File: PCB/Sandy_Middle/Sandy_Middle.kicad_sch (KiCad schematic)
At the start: 80 parts, among them J1 Conn_02x02_Top_Bottom, J2 Conn_02x02_Top_Bottom, J3 Conn_02x02_Top_Bottom

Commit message: ネジ穴のフットプリントをわかりやすく
これまでKiCadのライブラリに保存していたフットプリントを、ローカルへ移動。
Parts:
- H1, H10, H11, H12, H13, H14, H15, H16, H17, H18, H19, H2, H3, H4, H5, H6, H7, H8, H9: footprint MountingHole:MountingHole_2.2mm_M2_Pad_minimal -> locallib:MountingHole_2.2mm_M2_Pad_minimal

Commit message: ダイオードの方向を強調するシルクに変更
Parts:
- D1, D10, D11, D12, D13, D14, D15, D16, D17, D18, D2, D3, D4, D5, D6, D7, D8, D9: footprint Diode_SMD:D_SOD-123 -> locallib:D_SOD-123_Emphasized_Direction_Line
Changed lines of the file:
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@@
       (effects (font (size 1.27 1.27)) (justify right))
     )
-    (property "Footprint" "Diode_SMD:D_SOD-123" (id 2) (at 262.89 78.74 0)
+    (property "Footprint" "locallib:D_SOD-123_Emphasized_Direction_Line" (id 2) (at 262.89 78.74 0)
       (effects (font (size 1.27 1.27)) hide)
     )
@@
       (effects (font (size 1.27 1.27)) (justify right))
     )
-    (property "Footprint" "Diode_SMD:D_SOD-123" (id 2) (at 180.34 110.49 0)
+    (property "Footprint" "locallib:D_SOD-123_Emphasized_Direction_Line" (id 2) (at 180.34 110.49 0)
       (effects (font (size 1.27 1.27)) hide)
     )
@@
       (effects (font (size 1.27 1.27)) (justify right))
     )
-    (property "Footprint" "Diode_SMD:D_SOD-123" (id 2) (at 114.3 78.74 0)
+    (property "Footprint" "locallib:D_SOD-123_Emphasized_Direction_Line" (id 2) (at 114.3 78.74 0)
       (effects (font (size 1.27 1.27)) hide)
     )
@@
       (effects (font (size 1.27 1.27)) (justify right))
     )
-    (property "Footprint" "Diode_SMD:D_SOD-123" (id 2) (at 147.32 142.24 0)
+    (property "Footprint" "locallib:D_SOD-123_Emphasized_Direction_Line" (id 2) (at 147.32 142.24 0)
       (effects (font (size 1.27 1.27)) hide)
     )
@@
       (effects (font (size 1.27 1.27)) (justify right))
     )
-    (property "Footprint" "Diode_SMD:D_SOD-123" (id 2) (at 147.32 110.49 0)
+    (property "Footprint" "locallib:D_SOD-123_Emphasized_Direction_Line" (id 2) (at 147.32 110.49 0)
       (effects (font (size 1.27 1.27)) hide)
     )
@@
       (effects (font (size 1.27 1.27)) (justify right))
     )
-    (property "Footprint" "Diode_SMD:D_SOD-123" (id 2) (at 350.52 211.455 0)
+    (property "Footprint" "locallib:D_SOD-123_Emphasized_Direction_Line" (id 2) (at 350.52 211.455 0)
       (effects (font (size 1.27 1.27)) hide)
     )
@@
       (effects (font (size 1.27 1.27)) (justify right))
     )
-    (property "Footprint" "Diode_SMD:D_SOD-123" (id 2) (at 246.38 78.74 0)
+    (property "Footprint" "locallib:D_SOD-123_Emphasized_Direction_Line" (id 2) (at 246.38 78.74 0)
       (effects (font (size 1.27 1.27)) hide)
     )
@@
       (effects (font (size 1.27 1.27)) (justify right))
     )
-    (property "Footprint" "Diode_SMD:D_SOD-123" (id 2) (at 196.85 78.74 0)
+    (property "Footprint" "locallib:D_SOD-123_Emphasized_Direction_Line" (id 2) (at 196.85 78.74 0)
       (effects (font (size 1.27 1.27)) hide)
     )
@@
       (effects (font (size 1.27 1.27)) (justify right))
     )
-    (property "Footprint" "Diode_SMD:D_SOD-123" (id 2) (at 383.54 208.915 0)
+    (property "Footprint" "locallib:D_SOD-123_Emphasized_Direction_Line" (id 2) (at 383.54 208.915 0)
       (effects (font (size 1.27 1.27)) hide)
     )
@@
       (effects (font (size 1.27 1.27)) (justify right))
     )
-    (property "Footprint" "Diode_SMD:D_SOD-123" (id 2) (at 180.34 142.24 0)
+    (property "Footprint" "locallib:D_SOD-123_Emphasized_Direction_Line" (id 2) (at 180.34 142.24 0)
       (effects (font (size 1.27 1.27)) hide)
     )
@@
       (effects (font (size 1.27 1.27)) (justify right))
     )
-    (property "Footprint" "Diode_SMD:D_SOD-123" (id 2) (at 64.77 78.74 0)
+    (property "Footprint" "locallib:D_SOD-123_Emphasized_Direction_Line" (id 2) (at 64.77 78.74 0)
       (effects (font (size 1.27 1.27)) hide)
     )
@@
       (effects (font (size 1.27 1.27)) (justify right))
     )
-    (property "Footprint" "Diode_SMD:D_SOD-123" (id 2) (at 130.81 110.49 0)
+    (property "Footprint" "locallib:D_SOD-123_Emphasized_Direction_Line" (id 2) (at 130.81 110.49 0)
       (effects (font (size 1.27 1.27)) hide)
     )
@@
       (effects (font (size 1.27 1.27)) (justify right))
     )
-    (property "Footprint" "Diode_SMD:D_SOD-123" (id 2) (at 48.26 78.74 0)
+    (property "Footprint" "locallib:D_SOD-123_Emphasized_Direction_Line" (id 2) (at 48.26 78.74 0)
       (effects (font (size 1.27 1.27)) hide)
     )
@@
       (effects (font (size 1.27 1.27)) (justify right))
     )
-    (property "Footprint" "Diode_SMD:D_SOD-123" (id 2) (at 391.16 206.375 0)
+    (property "Footprint" "locallib:D_SOD-123_Emphasized_Direction_Line" (id 2) (at 391.16 206.375 0)
       (effects (font (size 1.27 1.27)) hide)
     )
@@
       (effects (font (size 1.27 1.27)) (justify right))
     )
-    (property "Footprint" "Diode_SMD:D_SOD-123" (id 2) (at 342.9 208.915 0)
+    (property "Footprint" "locallib:D_SOD-123_Emphasized_Direction_Line" (id 2) (at 342.9 208.915 0)
       (effects (font (size 1.27 1.27)) hide)
     )
@@
       (effects (font (size 1.27 1.27)) (justify right))
     )
-    (property "Footprint" "Diode_SMD:D_SOD-123" (id 2) (at 375.92 211.455 0)
+    (property "Footprint" "locallib:D_SOD-123_Emphasized_Direction_Line" (id 2) (at 375.92 211.455 0)
       (effects (font (size 1.27 1.27)) hide)
     )
@@
       (effects (font (size 1.27 1.27)) (justify right))
     )
-    (property "Footprint" "Diode_SMD:D_SOD-123" (id 2) (at 163.83 142.24 0)
+    (property "Footprint" "locallib:D_SOD-123_Emphasized_Direction_Line" (id 2) (at 163.83 142.24 0)
       (effects (font (size 1.27 1.27)) hide)
     )
@@
       (effects (font (size 1.27 1.27)) (justify right))
     )
-    (property "Footprint" "Diode_SMD:D_SOD-123" (id 2) (at 163.83 110.49 0)
+    (property "Footprint" "locallib:D_SOD-123_Emphasized_Direction_Line" (id 2) (at 163.83 110.49 0)
       (effects (font (size 1.27 1.27)) hide)
     )
@@
     )
     (path "/98a572f1-8857-4d32-9682-98d5a690baab"
-      (reference "D1") (unit 1) (value "D") (footprint "Diode_SMD:D_SOD-123")
+      (reference "D1") (unit 1) (value "D") (footprint "locallib:D_SOD-123_Emphasized_Direction_Line")
     )
     (path "/79b01d85-3e7e-49a5-baa8-c54e7a8ce4fa"
-      (reference "D2") (unit 1) (value "D") (footprint "Diode_SMD:D_SOD-123")
+      (reference "D2") (unit 1) (value "D") (footprint "locallib:D_SOD-123_Emphasized_Direction_Line")
     )
     (path "/10264225-1791-410d-9e41-7749c3624088"
-      (reference "D3") (unit 1) (value "D") (footprint "Diode_SMD:D_SOD-123")
+      (reference "D3") (unit 1) (value "D") (footprint "locallib:D_SOD-123_Emphasized_Direction_Line")
     )
     (path "/372e4b73-5697-4558-8707-c0918e154230"
-      (reference "D4") (unit 1) (value "D") (footprint "Diode_SMD:D_SOD-123")
+      (reference "D4") (unit 1) (value "D") (footprint "locallib:D_SOD-123_Emphasized_Direction_Line")
     )
     (path "/1e52539e-b1ab-4d88-9790-3c1108cb980e"
-      (reference "D5") (unit 1) (value "D") (footprint "Diode_SMD:D_SOD-123")
+      (reference "D5") (unit 1) (value "D") (footprint "locallib:D_SOD-123_Emphasized_Direction_Line")
     )
     (path "/02eb5dc3-9dab-4bdb-8773-510daf46eb56"
-      (reference "D6") (unit 1) (value "D") (footprint "Diode_SMD:D_SOD-123")
+      (reference "D6") (unit 1) (value "D") (footprint "locallib:D_SOD-123_Emphasized_Direction_Line")
     )
     (path "/7f4aa78f-d5fa-4df8-b529-c2e308c53e79"
-      (reference "D7") (unit 1) (value "D") (footprint "Diode_SMD:D_SOD-123")
+      (reference "D7") (unit 1) (value "D") (footprint "locallib:D_SOD-123_Emphasized_Direction_Line")
     )
     (path "/114f479f-c6d8-46a0-bd29-052d023e9b3d"
-      (reference "D8") (unit 1) (value "D") (footprint "Diode_SMD:D_SOD-123")
+      (reference "D8") (unit 1) (value "D") (footprint "locallib:D_SOD-123_Emphasized_Direction_Line")
     )
     (path "/fea2466c-e6a8-4101-8437-6f750141ce2c"
-      (reference "D9") (unit 1) (value "D") (footprint "Diode_SMD:D_SOD-123")
+      (reference "D9") (unit 1) (value "D") (footprint "locallib:D_SOD-123_Emphasized_Direction_Line")
     )
     (path "/05274209-3705-4225-9924-d5d2588282b9"
-      (reference "D10") (unit 1) (value "D") (footprint "Diode_SMD:D_SOD-123")
+      (reference "D10") (unit 1) (value "D") (footprint "locallib:D_SOD-123_Emphasized_Direction_Line")
     )
     (path "/114627db-0c52-4502-94e0-058f1357fd45"
-      (reference "D11") (unit 1) (value "D") (footprint "Diode_SMD:D_SOD-123")
+      (reference "D11") (unit 1) (value "D") (footprint "locallib:D_SOD-123_Emphasized_Direction_Line")
     )
     (path "/e73a99b3-45a4-48e4-b59e-5c57a9a725ce"
-      (reference "D12") (unit 1) (value "D") (footprint "Diode_SMD:D_SOD-123")
+      (reference "D12") (unit 1) (value "D") (footprint "locallib:D_SOD-123_Emphasized_Direction_Line")
     )
     (path "/40013a98-70f3-4e35-90ce-3840d3806235"
-      (reference "D13") (unit 1) (value "D") (footprint "Diode_SMD:D_SOD-123")
+      (reference "D13") (unit 1) (value "D") (footprint "locallib:D_SOD-123_Emphasized_Direction_Line")
     )
     (path "/9f424bf6-d591-4ef8-ab26-5de921e524da"
-      (reference "D14") (unit 1) (value "D") (footprint "Diode_SMD:D_SOD-123")
+      (reference "D14") (unit 1) (value "D") (footprint "locallib:D_SOD-123_Emphasized_Direction_Line")
     )
     (path "/a92d7c5f-b604-465e-a4c5-bd808af5ea5f"
-      (reference "D15") (unit 1) (value "D") (footprint "Diode_SMD:D_SOD-123")
+      (reference "D15") (unit 1) (value "D") (footprint "locallib:D_SOD-123_Emphasized_Direction_Line")
     )
     (path "/3c9dd9f6-196b-4ea2-bd2f-322451f5fe46"
-      (reference "D16") (unit 1) (value "D") (footprint "Diode_SMD:D_SOD-123")
+      (reference "D16") (unit 1) (value "D") (footprint "locallib:D_SOD-123_Emphasized_Direction_Line")
     )
     (path "/1680d709-e50f-4ff9-ada3-4903ce086e07"
-      (reference "D17") (unit 1) (value "D") (footprint "Diode_SMD:D_SOD-123")
+      (reference "D17") (unit 1) (value "D") (footprint "locallib:D_SOD-123_Emphasized_Direction_Line")
     )
     (path "/af171445-bb08-40d9-9b16-1214459bb813"
-      (reference "D18") (unit 1) (value "D") (footprint "Diode_SMD:D_SOD-123")
+      (reference "D18") (unit 1) (value "D") (footprint "locallib:D_SOD-123_Emphasized_Direction_Line")
     )
     (path "/957451e1-7977-4bf5-b4a7-01d7dbc16c20"

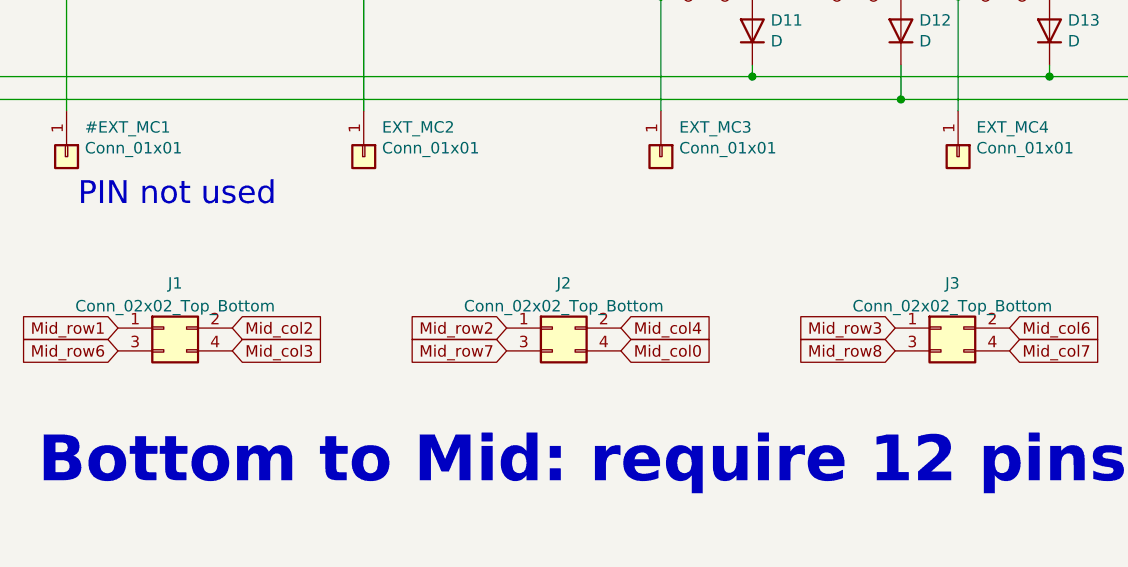
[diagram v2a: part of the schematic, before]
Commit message: コネクタの番号と、パーツの番号を合わせる
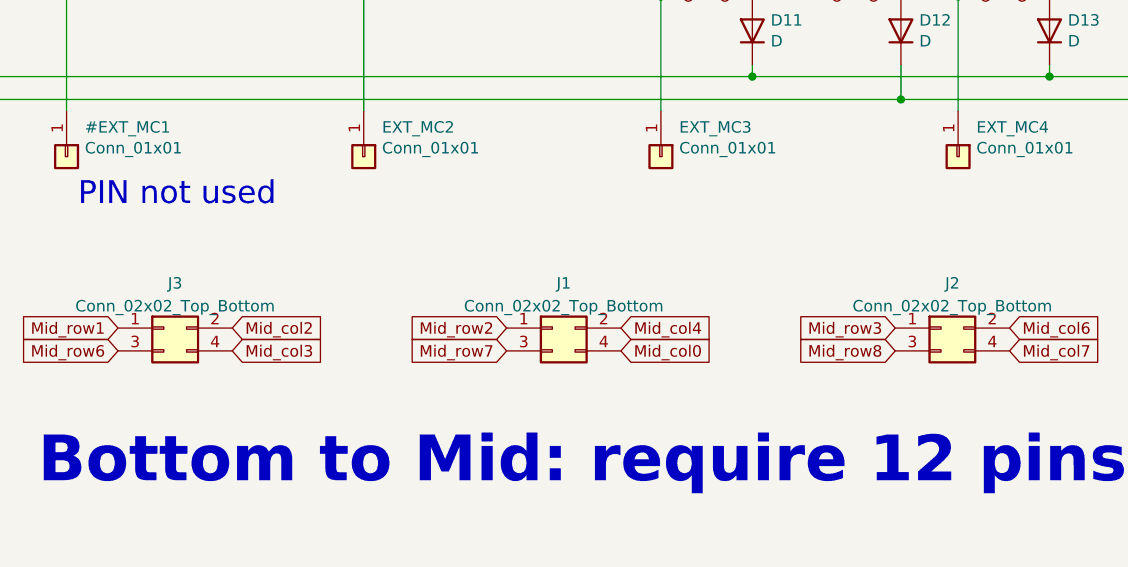
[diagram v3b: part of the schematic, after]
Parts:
- renumbered J2 to J1, J3 to J2, J1 to J3
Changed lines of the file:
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@@
   (symbol (lib_id "Connector_Generic:Conn_02x02_Odd_Even") (at 168.275 175.26 0) (unit 1)
     (in_bom yes) (on_board yes) (fields_autoplaced)
-    (property "Reference" "J3" (id 0) (at 169.545 170.2902 0))
+    (property "Reference" "J2" (id 0) (at 169.545 170.2902 0))
     (property "Value" "Conn_02x02_Top_Bottom" (id 1) (at 169.545 172.8271 0))
     (property "Footprint" "locallib:JST_SH_SM04B-SRSS-TB_1x04-1MP_P1.00mm_Horizontal_wCable_housing_spare_pin" (id 2) (at 168.275 175.26 0)
@@
   (symbol (lib_id "Connector_Generic:Conn_02x02_Odd_Even") (at 125.095 175.26 0) (unit 1)
     (in_bom yes) (on_board yes) (fields_autoplaced)
-    (property "Reference" "J2" (id 0) (at 126.365 170.2902 0))
+    (property "Reference" "J1" (id 0) (at 126.365 170.2902 0))
     (property "Value" "Conn_02x02_Top_Bottom" (id 1) (at 126.365 172.8271 0))
     (property "Footprint" "locallib:JST_SH_SM04B-SRSS-TB_1x04-1MP_P1.00mm_Horizontal_wCable_housing_spare_pin" (id 2) (at 125.095 175.26 0)
@@
   (symbol (lib_id "Connector_Generic:Conn_02x02_Odd_Even") (at 81.915 175.26 0) (unit 1)
     (in_bom yes) (on_board yes) (fields_autoplaced)
-    (property "Reference" "J1" (id 0) (at 83.185 170.2902 0))
+    (property "Reference" "J3" (id 0) (at 83.185 170.2902 0))
     (property "Value" "Conn_02x02_Top_Bottom" (id 1) (at 83.185 172.8271 0))
     (property "Footprint" "locallib:JST_SH_SM04B-SRSS-TB_1x04-1MP_P1.00mm_Horizontal_wCable_housing_spare_pin" (id 2) (at 81.915 175.26 0)
@@
       (reference "H19") (unit 1) (value "MountingHole") (footprint "locallib:MountingHole_2.2mm_M2_Pad_minimal")
     )
+    (path "/241d68cd-559c-443d-9f6d-2e6949462e93"
+      (reference "J1") (unit 1) (value "Conn_02x02_Top_Bottom") (footprint "locallib:JST_SH_SM04B-SRSS-TB_1x04-1MP_P1.00mm_Horizontal_wCable_housing_spare_pin")
+    )
+    (path "/1fd773fe-f658-4a6a-aeb7-315c3cfd0eee"
+      (reference "J2") (unit 1) (value "Conn_02x02_Top_Bottom") (footprint "locallib:JST_SH_SM04B-SRSS-TB_1x04-1MP_P1.00mm_Horizontal_wCable_housing_spare_pin")
+    )
     (path "/8f11b508-47a9-405d-924f-c9833af03b08"
-      (reference "J1") (unit 1) (value "Conn_02x02_Top_Bottom") (footprint "locallib:JST_SH_SM04B-SRSS-TB_1x04-1MP_P1.00mm_Horizontal_wCable_housing_spare_pin")
-    )
-    (path "/241d68cd-559c-443d-9f6d-2e6949462e93"
-      (reference "J2") (unit 1) (value "Conn_02x02_Top_Bottom") (footprint "locallib:JST_SH_SM04B-SRSS-TB_1x04-1MP_P1.00mm_Horizontal_wCable_housing_spare_pin")
-    )
-    (path "/1fd773fe-f658-4a6a-aeb7-315c3cfd0eee"
       (reference "J3") (unit 1) (value "Conn_02x02_Top_Bottom") (footprint "locallib:JST_SH_SM04B-SRSS-TB_1x04-1MP_P1.00mm_Horizontal_wCable_housing_spare_pin")
     )

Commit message: SHコネクタのパーツ番号を追加
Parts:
- J1, J2, J3: LCSC (none) -> C371510
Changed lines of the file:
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@@
+      (effects (font (size 1.27 1.27)) hide)
+    )
+    (property "LCSC" "C371510" (id 4) (at 168.275 175.26 0)
       (effects (font (size 1.27 1.27)) hide)
     )
@@
       (effects (font (size 1.27 1.27)) hide)
     )
+    (property "LCSC" "C371510" (id 4) (at 125.095 175.26 0)
+      (effects (font (size 1.27 1.27)) hide)
+    )
     (pin "1")
     (pin "2")
@@
       (effects (font (size 1.27 1.27)) hide)
     )
+    (property "LCSC" "C371510" (id 4) (at 81.915 175.26 0)
+      (effects (font (size 1.27 1.27)) hide)
+    )

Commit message: Mid v02（外形変更はまだ）
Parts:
- removed D14, D15, D16, D17, D18: D, locallib:D_SOD-123_Emphasized_Direction_Line, symbol Device:D
- removed S1: JS5208, locallib:SW_JS5208_add_MP_hole_one_hole, symbol JS5208:JS5208
- removed SW_TAB1.25u1: SW_Push, MX_Alps_Hybrid:MXOnly-1.25U-NoLED, symbol Switch:SW_Push
- SW_'1, SW_;1, SW_G1, SW_H1, SW_P1, SW_Q1, SW_R1, SW_R4CenterC1, SW_R4CenterL1, SW_R4CenterR1, SW_U1: footprint MX_Alps_Hybrid:MXOnly-1U-NoLED -> MX_Alps_Hybrid:MXOnly-1U-Hotswap-guide
- SW_BS1.5u1, SW_TAB1.5u1: footprint MX_Alps_Hybrid:MXOnly-1.5U-NoLED -> MX_Alps_Hybrid:MXOnly-1.5U-Hotswap-guide
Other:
- note removed: "5-way navigation switch"

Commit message: MiddleをSMTAした場合の製造費確認用ファイル出力
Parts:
- J1, J2, J3: LCSC C371510 -> C160404
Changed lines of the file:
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@@
       (effects (font (size 1.27 1.27)) hide)
     )
-    (property "LCSC" "C371510" (at 168.275 175.26 0)
+    (property "LCSC" "C160404" (at 168.275 175.26 0)
       (effects (font (size 1.27 1.27)) hide)
     )
@@
       (effects (font (size 1.27 1.27)) hide)
     )
-    (property "LCSC" "C371510" (at 125.095 175.26 0)
+    (property "LCSC" "C160404" (at 125.095 175.26 0)
       (effects (font (size 1.27 1.27)) hide)
     )
@@
       (effects (font (size 1.27 1.27)) hide)
     )
-    (property "LCSC" "C371510" (at 81.915 175.26 0)
-      (effects (font (size 1.27 1.27)) hide)
-    )
+    (property "LCSC" "C160404" (at 81.915 175.26 0)
+      (effects (font (size 1.27 1.27)) hide)
+    )
